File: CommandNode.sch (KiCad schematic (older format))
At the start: 0 parts

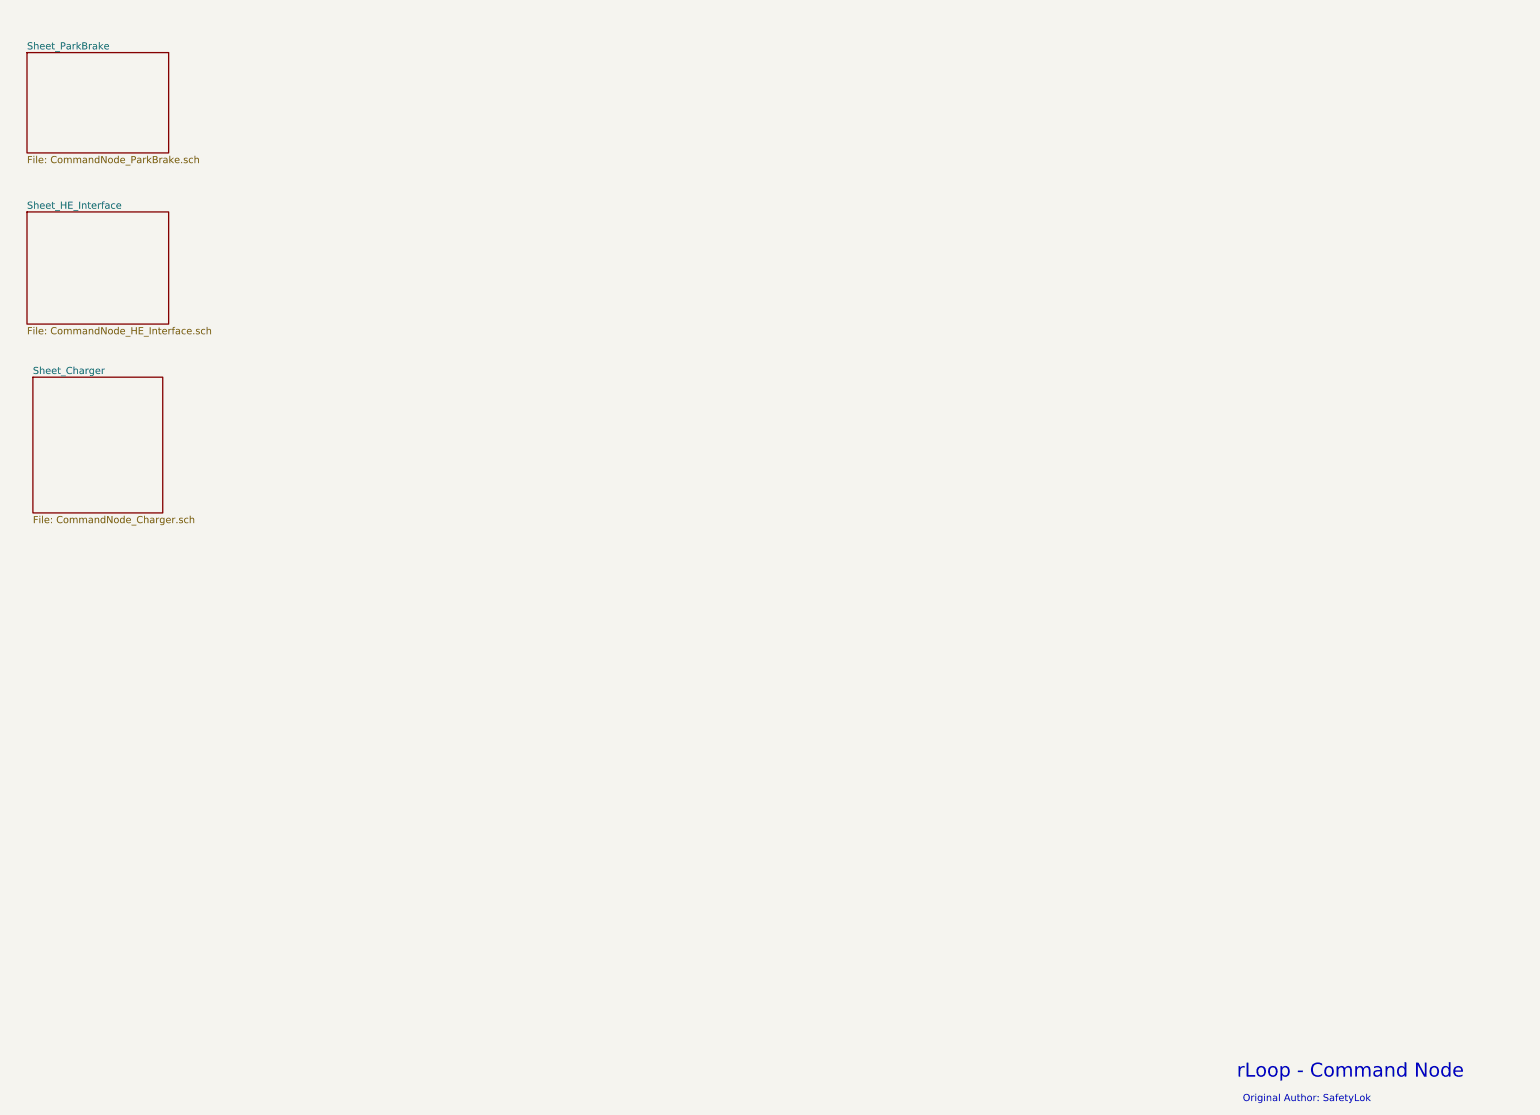
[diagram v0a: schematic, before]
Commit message: Created isolated RS585 interfaces and completed park brake.
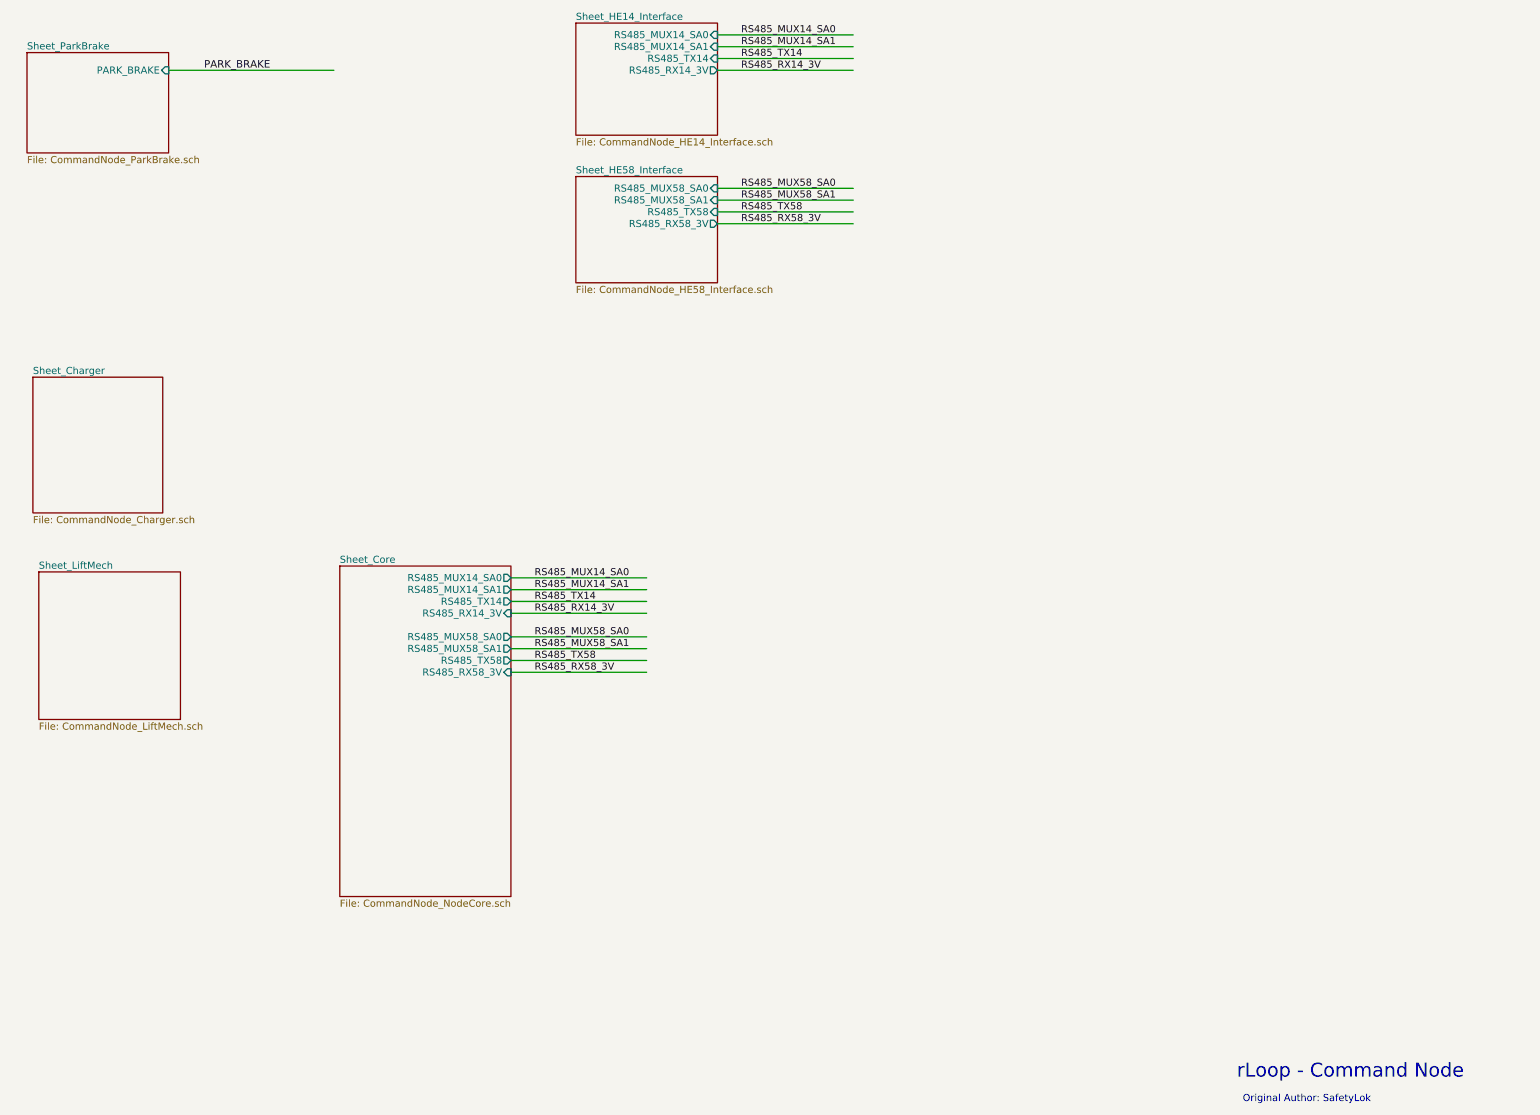
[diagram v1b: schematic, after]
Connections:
- net labels added: PARK_BRAKE, RS485_MUX14_SA0, RS485_MUX14_SA1, RS485_MUX58_SA0, RS485_MUX58_SA1, RS485_RX14_3V, RS485_RX58_3V, RS485_TX14, RS485_TX58
- wire segments 0 -> 17
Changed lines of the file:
@@
 LIBS:contrib
 LIBS:valves
+LIBS:rloop
 LIBS:CommandNode-cache
 EELAYER 25 0
@@
 $Descr A3 16535 11693
 encoding utf-8
-Sheet 1 4
+Sheet 1 7
 Title "Command Node - Overview"
 Date ""
@@
 F0 "Sheet_ParkBrake" 60
 F1 "CommandNode_ParkBrake.sch" 60
+F2 "PARK_BRAKE" I R 2900 1600 60
 $EndSheet
 $Sheet
-S 1700 2800 1200 950
+S 6350 1200 1200 950
 U 5753E2F1
-F0 "Sheet_HE_Interface" 60
-F1 "CommandNode_HE_Interface.sch" 60
+F0 "Sheet_HE14_Interface" 60
+F1 "CommandNode_HE14_Interface.sch" 60
+F2 "RS485_MUX14_SA0" I R 7550 1300 60
+F3 "RS485_MUX14_SA1" I R 7550 1400 60
+F4 "RS485_TX14" I R 7550 1500 60
+F5 "RS485_RX14_3V" O R 7550 1600 60
 $EndSheet
 $Sheet
@@
 F1 "CommandNode_Charger.sch" 60
 $EndSheet
+$Sheet
+S 1800 5850 1200 1250
+U 575CB3DC
+F0 "Sheet_LiftMech" 60
+F1 "CommandNode_LiftMech.sch" 60
+$EndSheet
+$Sheet
+S 4350 5800 1450 2800
+U 575CB3EF
+F0 "Sheet_Core" 60
+F1 "CommandNode_NodeCore.sch" 60
+F2 "RS485_MUX14_SA0" O R 5800 5900 60
+F3 "RS485_MUX14_SA1" O R 5800 6000 60
+F4 "RS485_TX14" O R 5800 6100 60
+F5 "RS485_RX14_3V" I R 5800 6200 60
+F6 "RS485_MUX58_SA0" O R 5800 6400 60
+F7 "RS485_MUX58_SA1" O R 5800 6500 60
+F8 "RS485_TX58" O R 5800 6600 60
+F9 "RS485_RX58_3V" I R 5800 6700 60
+$EndSheet
+$Sheet
+S 6350 2500 1200 900
+U 575D589B
+F0 "Sheet_HE58_Interface" 60
+F1 "CommandNode_HE58_Interface.sch" 60
+F2 "RS485_MUX58_SA0" I R 7550 2600 60
+F3 "RS485_MUX58_SA1" I R 7550 2700 60
+F4 "RS485_TX58" I R 7550 2800 60
+F5 "RS485_RX58_3V" O R 7550 2900 60
+$EndSheet
+Wire Wire Line
+	5800 5900 6950 5900
+Wire Wire Line
+	5800 6000 6950 6000
+Wire Wire Line
+	5800 6100 6950 6100
+Wire Wire Line
+	5800 6200 6950 6200
+Wire Wire Line
+	5800 6400 6950 6400
+Wire Wire Line
+	5800 6500 6950 6500
+Wire Wire Line
+	5800 6600 6950 6600
+Wire Wire Line
+	5800 6700 6950 6700
+Text Label 6000 5900 0    60   ~ 0
+RS485_MUX14_SA0
+Text Label 6000 6000 0    60   ~ 0
+RS485_MUX14_SA1
+Text Label 6000 6400 0    60   ~ 0
+RS485_MUX58_SA0
+Text Label 6000 6500 0    60   ~ 0
+RS485_MUX58_SA1
+Text Label 6000 6100 0    60   ~ 0
+RS485_TX14
+Text Label 6000 6600 0    60   ~ 0
+RS485_TX58
+Text Label 6000 6200 0    60   ~ 0
+RS485_RX14_3V
+Text Label 6000 6700 0    60   ~ 0
+RS485_RX58_3V
+Wire Wire Line
+	7550 1300 8700 1300
+Wire Wire Line
+	7550 1400 8700 1400
+Wire Wire Line
+	7550 1500 8700 1500
+Wire Wire Line
+	7550 1600 8700 1600
+Text Label 7750 1300 0    60   ~ 0
+RS485_MUX14_SA0
+Text Label 7750 1400 0    60   ~ 0
+RS485_MUX14_SA1
+Text Label 7750 1500 0    60   ~ 0
+RS485_TX14
+Text Label 7750 1600 0    60   ~ 0
+RS485_RX14_3V
+Wire Wire Line
+	7550 2600 8700 2600
+Wire Wire Line
+	7550 2700 8700 2700
+Wire Wire Line
+	7550 2800 8700 2800
+Wire Wire Line
+	7550 2900 8700 2900
+Text Label 7750 2600 0    60   ~ 0
+RS485_MUX58_SA0
+Text Label 7750 2700 0    60   ~ 0
+RS485_MUX58_SA1
+Text Label 7750 2800 0    60   ~ 0
+RS485_TX58
+Text Label 7750 2900 0    60   ~ 0
+RS485_RX58_3V
+Wire Wire Line
+	2900 1600 4300 1600
+Text Label 3200 1600 0    63   ~ 0
+PARK_BRAKE
 $EndSCHEMATC

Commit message: Finish and print schematics for review
Lifting mechanism, charger interface, Data Enable on HE controller
RS585, Park Brake and node core.
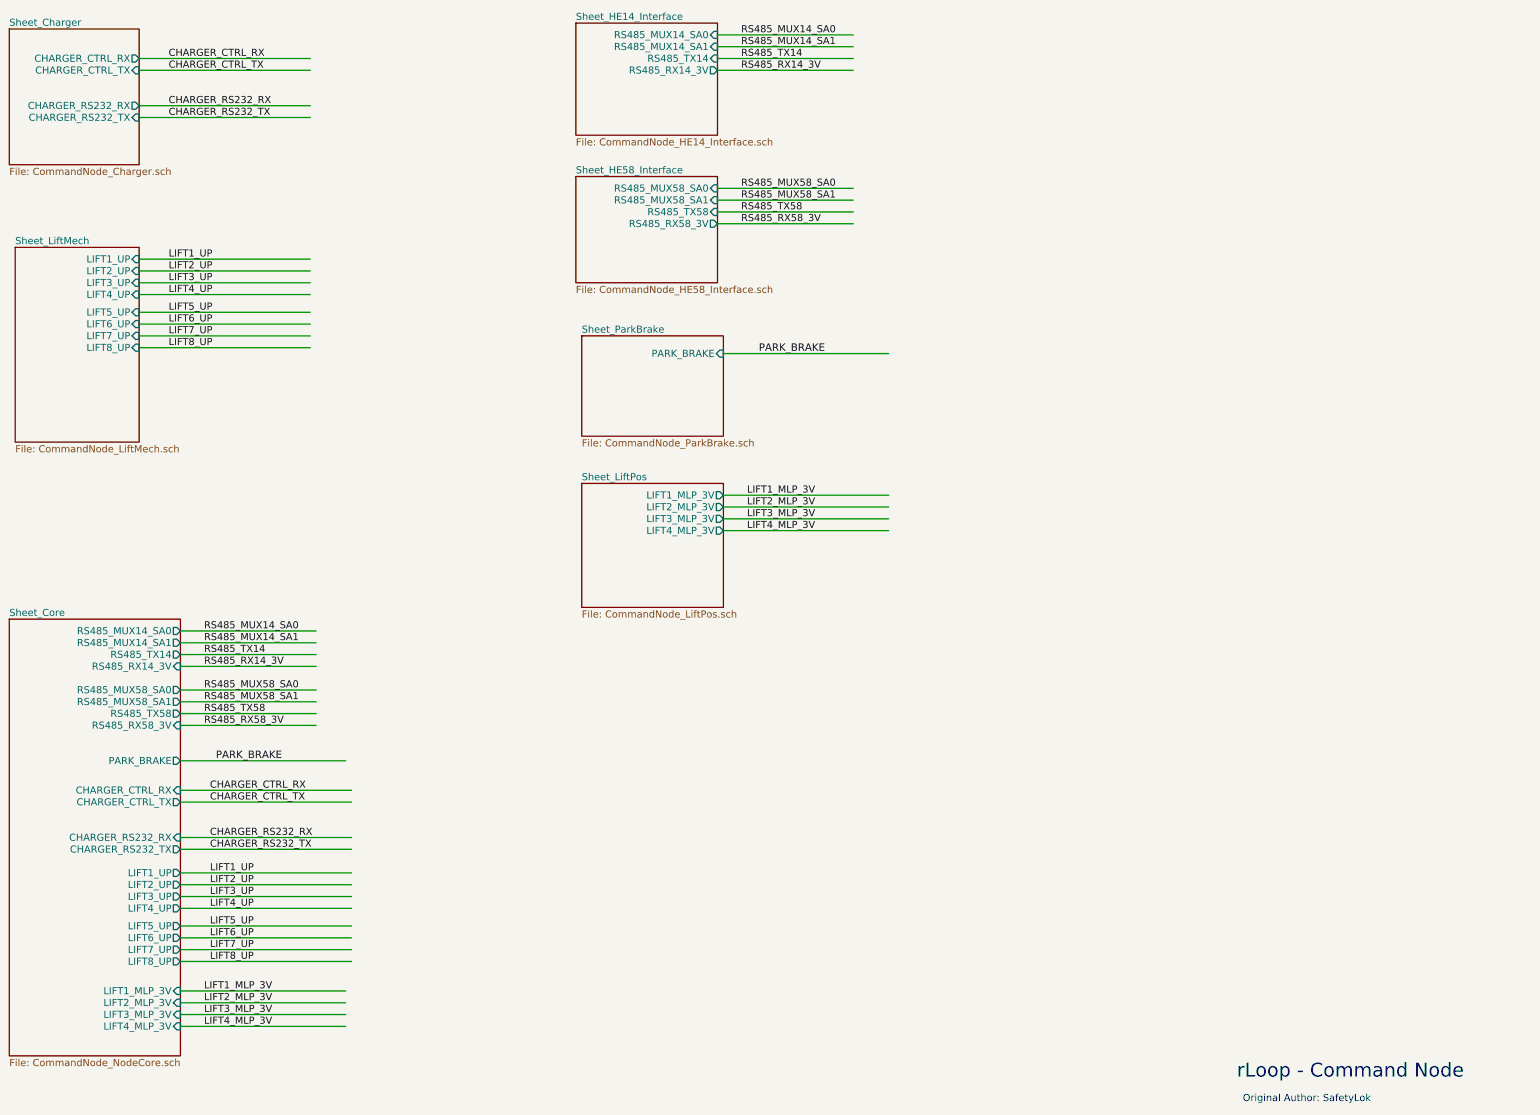
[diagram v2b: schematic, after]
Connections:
- net labels added: CHARGER_CTRL_RX, CHARGER_CTRL_TX, CHARGER_RS232_RX, CHARGER_RS232_TX, LIFT1_MLP_3V, LIFT1_UP, LIFT2_MLP_3V, LIFT2_UP, LIFT3_MLP_3V, LIFT3_UP, LIFT4_MLP_3V, LIFT4_UP, LIFT5_UP, LIFT6_UP, LIFT7_UP, LIFT8_UP
- wire segments 17 -> 50
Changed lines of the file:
@@
 $Descr A3 16535 11693
 encoding utf-8
-Sheet 1 7
+Sheet 1 8
 Title "Command Node - Overview"
 Date ""
@@
 Original Author: SafetyLok
 $Sheet
-S 1700 1450 1200 850
+S 6400 3850 1200 850
 U 5753E2BE
 F0 "Sheet_ParkBrake" 60
 F1 "CommandNode_ParkBrake.sch" 60
-F2 "PARK_BRAKE" I R 2900 1600 60
+F2 "PARK_BRAKE" I R 7600 4000 60
 $EndSheet
 $Sheet
@@
 $EndSheet
 $Sheet
-S 1750 4200 1100 1150
+S 1550 1250 1100 1150
 U 5753E306
 F0 "Sheet_Charger" 60
 F1 "CommandNode_Charger.sch" 60
-$EndSheet
-$Sheet
-S 1800 5850 1200 1250
+F2 "CHARGER_CTRL_TX" I R 2650 1600 60
+F3 "CHARGER_RS232_RX" O R 2650 1900 60
+F4 "CHARGER_CTRL_RX" O R 2650 1500 60
+F5 "CHARGER_RS232_TX" I R 2650 2000 60
+$EndSheet
+$Sheet
+S 1600 3100 1050 1650
 U 575CB3DC
 F0 "Sheet_LiftMech" 60
 F1 "CommandNode_LiftMech.sch" 60
-$EndSheet
-$Sheet
-S 4350 5800 1450 2800
+F2 "LIFT5_UP" I R 2650 3650 60
+F3 "LIFT6_UP" I R 2650 3750 60
+F4 "LIFT7_UP" I R 2650 3850 60
+F5 "LIFT8_UP" I R 2650 3950 60
+F6 "LIFT1_UP" I R 2650 3200 60
+F7 "LIFT2_UP" I R 2650 3300 60
+F8 "LIFT3_UP" I R 2650 3400 60
+F9 "LIFT4_UP" I R 2650 3500 60
+$EndSheet
+$Sheet
+S 1550 6250 1450 3700
 U 575CB3EF
 F0 "Sheet_Core" 60
 F1 "CommandNode_NodeCore.sch" 60
-F2 "RS485_MUX14_SA0" O R 5800 5900 60
-F3 "RS485_MUX14_SA1" O R 5800 6000 60
-F4 "RS485_TX14" O R 5800 6100 60
-F5 "RS485_RX14_3V" I R 5800 6200 60
-F6 "RS485_MUX58_SA0" O R 5800 6400 60
-F7 "RS485_MUX58_SA1" O R 5800 6500 60
-F8 "RS485_TX58" O R 5800 6600 60
-F9 "RS485_RX58_3V" I R 5800 6700 60
+F2 "RS485_MUX14_SA0" O R 3000 6350 60
+F3 "RS485_MUX14_SA1" O R 3000 6450 60
+F4 "RS485_TX14" O R 3000 6550 60
+F5 "RS485_RX14_3V" I R 3000 6650 60
+F6 "RS485_MUX58_SA0" O R 3000 6850 60
+F7 "RS485_MUX58_SA1" O R 3000 6950 60
+F8 "RS485_TX58" O R 3000 7050 60
+F9 "RS485_RX58_3V" I R 3000 7150 60
+F10 "PARK_BRAKE" O R 3000 7450 60
+F11 "CHARGER_CTRL_TX" O R 3000 7800 60
+F12 "CHARGER_RS232_RX" I R 3000 8100 60
+F13 "CHARGER_CTRL_RX" I R 3000 7700 60
+F14 "CHARGER_RS232_TX" O R 3000 8200 60
+F15 "LIFT1_UP" O R 3000 8400 60
+F16 "LIFT2_UP" O R 3000 8500 60
+F17 "LIFT3_UP" O R 3000 8600 60
+F18 "LIFT4_UP" O R 3000 8700 60
+F19 "LIFT5_UP" O R 3000 8850 60
+F20 "LIFT6_UP" O R 3000 8950 60
+F21 "LIFT7_UP" O R 3000 9050 60
+F22 "LIFT8_UP" O R 3000 9150 60
+F23 "LIFT1_MLP_3V" I R 3000 9400 60
+F24 "LIFT2_MLP_3V" I R 3000 9500 60
+F25 "LIFT3_MLP_3V" I R 3000 9600 60
+F26 "LIFT4_MLP_3V" I R 3000 9700 60
 $EndSheet
 $Sheet
@@
 $EndSheet
 Wire Wire Line
-	5800 5900 6950 5900
-Wire Wire Line
-	5800 6000 6950 6000
-Wire Wire Line
-	5800 6100 6950 6100
-Wire Wire Line
-	5800 6200 6950 6200
-Wire Wire Line
-	5800 6400 6950 6400
-Wire Wire Line
-	5800 6500 6950 6500
-Wire Wire Line
-	5800 6600 6950 6600
-Wire Wire Line
-	5800 6700 6950 6700
-Text Label 6000 5900 0    60   ~ 0
+	3000 6350 4150 6350
+Wire Wire Line
+	3000 6450 4150 6450
+Wire Wire Line
+	3000 6550 4150 6550
+Wire Wire Line
+	3000 6650 4150 6650
+Wire Wire Line
+	3000 6850 4150 6850
+Wire Wire Line
+	3000 6950 4150 6950
+Wire Wire Line
+	3000 7050 4150 7050
+Wire Wire Line
+	3000 7150 4150 7150
+Text Label 3200 6350 0    60   ~ 0
 RS485_MUX14_SA0
-Text Label 6000 6000 0    60   ~ 0
+Text Label 3200 6450 0    60   ~ 0
 RS485_MUX14_SA1
-Text Label 6000 6400 0    60   ~ 0
+Text Label 3200 6850 0    60   ~ 0
 RS485_MUX58_SA0
-Text Label 6000 6500 0    60   ~ 0
+Text Label 3200 6950 0    60   ~ 0
 RS485_MUX58_SA1
-Text Label 6000 6100 0    60   ~ 0
+Text Label 3200 6550 0    60   ~ 0
 RS485_TX14
-Text Label 6000 6600 0    60   ~ 0
+Text Label 3200 7050 0    60   ~ 0
 RS485_TX58
-Text Label 6000 6200 0    60   ~ 0
+Text Label 3200 6650 0    60   ~ 0
 RS485_RX14_3V
-Text Label 6000 6700 0    60   ~ 0
+Text Label 3200 7150 0    60   ~ 0
 RS485_RX58_3V
 Wire Wire Line
@@
 RS485_RX58_3V
 Wire Wire Line
-	2900 1600 4300 1600
-Text Label 3200 1600 0    63   ~ 0
+	7600 4000 9000 4000
+Text Label 7900 4000 0    63   ~ 0
 PARK_BRAKE
+Wire Wire Line
+	2650 1500 4100 1500
+Text Label 2900 1500 0    60   ~ 0
+CHARGER_CTRL_RX
+Wire Wire Line
+	2650 1600 4100 1600
+Text Label 2900 1600 0    60   ~ 0
+CHARGER_CTRL_TX
+Wire Wire Line
+	2650 1900 4100 1900
+Wire Wire Line
+	2650 2000 4100 2000
+Text Label 2900 1900 0    60   ~ 0
+CHARGER_RS232_RX
+Text Label 2900 2000 0    60   ~ 0
+CHARGER_RS232_TX
+Wire Wire Line
+	3000 7450 4400 7450
+Text Label 3300 7450 0    63   ~ 0
+PARK_BRAKE
+Wire Wire Line
+	3000 7700 4450 7700
+Text Label 3250 7700 0    60   ~ 0
+CHARGER_CTRL_RX
+Wire Wire Line
+	3000 7800 4450 7800
+Text Label 3250 7800 0    60   ~ 0
+CHARGER_CTRL_TX
+Wire Wire Line
+	3000 8100 4450 8100
+Wire Wire Line
+	3000 8200 4450 8200
+Text Label 3250 8100 0    60   ~ 0
+CHARGER_RS232_RX
+Text Label 3250 8200 0    60   ~ 0
+CHARGER_RS232_TX
+Wire Wire Line
+	2650 3200 4100 3200
+Wire Wire Line
+	2650 3300 4100 3300
+Text Label 2900 3200 0    60   ~ 0
+LIFT1_UP
+Text Label 2900 3300 0    60   ~ 0
+LIFT2_UP
+Wire Wire Line
+	2650 3400 4100 3400
+Wire Wire Line
+	2650 3500 4100 3500
+Text Label 2900 3400 0    60   ~ 0
+LIFT3_UP
+Text Label 2900 3500 0    60   ~ 0
+LIFT4_UP
+Wire Wire Line
+	2650 3650 4100 3650
+Wire Wire Line
+	2650 3750 4100 3750
+Text Label 2900 3650 0    60   ~ 0
+LIFT5_UP
+Text Label 2900 3750 0    60   ~ 0
+LIFT6_UP
+Wire Wire Line
+	2650 3850 4100 3850
+Wire Wire Line
+	2650 3950 4100 3950
+Text Label 2900 3850 0    60   ~ 0
+LIFT7_UP
+Text Label 2900 3950 0    60   ~ 0
+LIFT8_UP
+Wire Wire Line
+	3000 8400 4450 8400
+Wire Wire Line
+	3000 8500 4450 8500
+Text Label 3250 8400 0    60   ~ 0
+LIFT1_UP
+Text Label 3250 8500 0    60   ~ 0
+LIFT2_UP
+Wire Wire Line
+	3000 8600 4450 8600
+Wire Wire Line
+	3000 8700 4450 8700
+Text Label 3250 8600 0    60   ~ 0
+LIFT3_UP
+Text Label 3250 8700 0    60   ~ 0
+LIFT4_UP
+Wire Wire Line
+	3000 8850 4450 8850
+Wire Wire Line
+	3000 8950 4450 8950
+Text Label 3250 8850 0    60   ~ 0
+LIFT5_UP
+Text Label 3250 8950 0    60   ~ 0
+LIFT6_UP
+Wire Wire Line
+	3000 9050 4450 9050
+Wire Wire Line
+	3000 9150 4450 9150
+Text Label 3250 9050 0    60   ~ 0
+LIFT7_UP
+Text Label 3250 9150 0    60   ~ 0
+LIFT8_UP
+$Sheet
+S 6400 5100 1200 1050
+U 576B1897
+F0 "Sheet_LiftPos" 60
+F1 "CommandNode_LiftPos.sch" 60
+F2 "LIFT1_MLP_3V" O R 7600 5200 60
+F3 "LIFT2_MLP_3V" O R 7600 5300 60
+F4 "LIFT3_MLP_3V" O R 7600 5400 60
+F5 "LIFT4_MLP_3V" O R 7600 5500 60
+$EndSheet
+Wire Wire Line
+	7600 5200 9000 5200
+Text Label 7800 5200 0    60   ~ 0
+LIFT1_MLP_3V
+Wire Wire Line
+	7600 5300 9000 5300
+Text Label 7800 5300 0    60   ~ 0
+LIFT2_MLP_3V
+Wire Wire Line
+	7600 5400 9000 5400
+Text Label 7800 5400 0    60   ~ 0
+LIFT3_MLP_3V
+Wire Wire Line
+	7600 5500 9000 5500
+Text Label 7800 5500 0    60   ~ 0
+LIFT4_MLP_3V
+Wire Wire Line
+	3000 9400 4400 9400
+Text Label 3200 9400 0    60   ~ 0
+LIFT1_MLP_3V
+Wire Wire Line
+	3000 9500 4400 9500
+Text Label 3200 9500 0    60   ~ 0
+LIFT2_MLP_3V
+Wire Wire Line
+	3000 9600 4400 9600
+Text Label 3200 9600 0    60   ~ 0
+LIFT3_MLP_3V
+Wire Wire Line
+	3000 9700 4400 9700
+Text Label 3200 9700 0    60   ~ 0
+LIFT4_MLP_3V
 $EndSCHEMATC
